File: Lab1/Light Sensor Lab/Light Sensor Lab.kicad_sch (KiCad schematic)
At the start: 9 parts, among them J1 Conn_01x03, U1 LMC6482

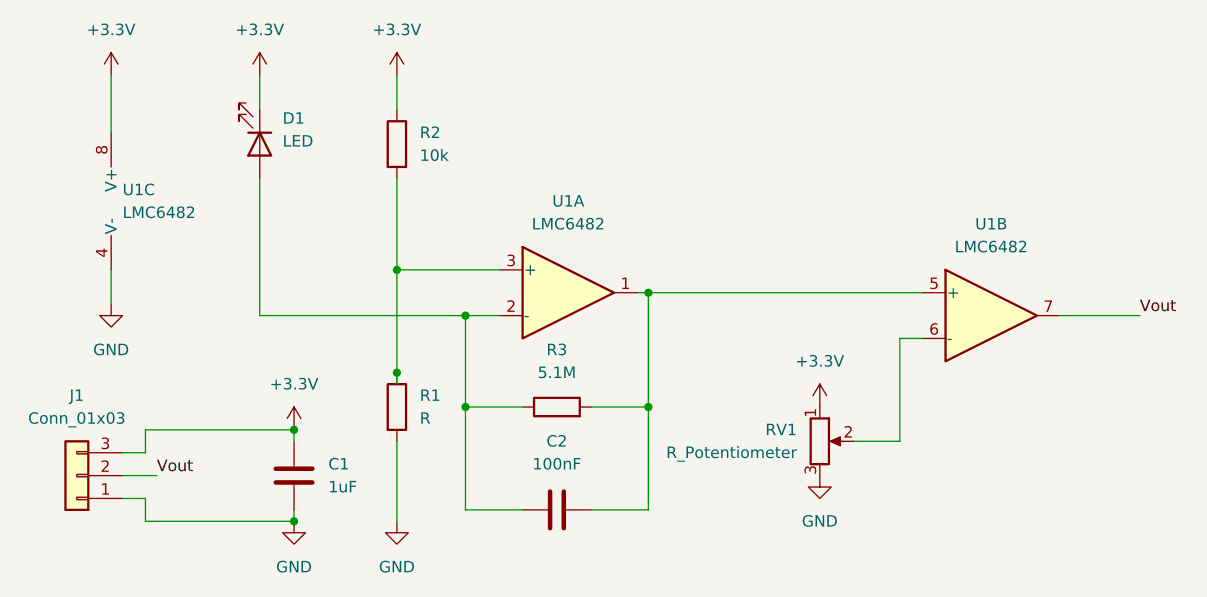
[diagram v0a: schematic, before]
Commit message: added PWR_FLAG for ERC
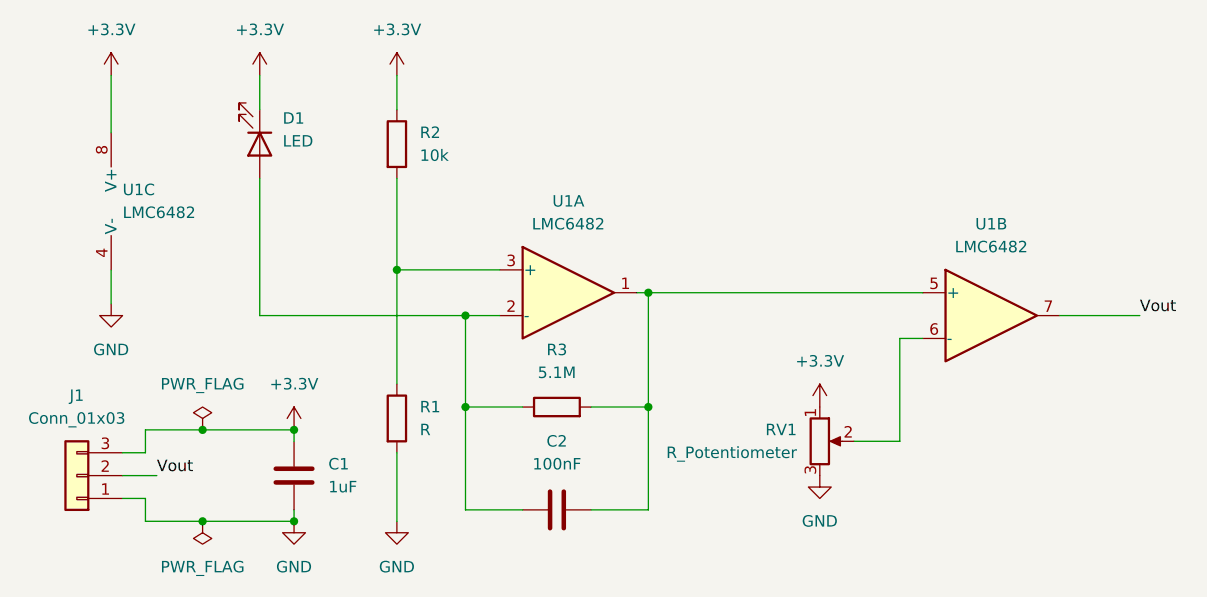
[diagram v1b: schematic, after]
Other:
- moved on the sheet: R1

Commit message: Finished Schematic And Checked Off
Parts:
- R1: value R -> 10k
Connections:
- net +3.3V: now also J1.1 (Pin_1), RV1.3; no longer J1.3 (Pin_3), RV1.1
- net GND: now also J1.3 (Pin_3), RV1.1; no longer J1.1 (Pin_1), RV1.3
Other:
- moved on the sheet: J1
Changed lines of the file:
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@@
+	(wire
+		(pts
+			(xy 153.67 101.6) (xy 153.67 104.14)
+		)
+		(stroke
+			(width 0)
+			(type default)
+		)
+	)
 	(wire
 		(pts
 			(xy 78.74 114.3) (xy 78.74 116.84)
+		)
+		(stroke
+			(width 0)
+			(type default)
+		)
+	)
+	(wire
+		(pts
+			(xy 153.67 114.3) (xy 153.67 111.76)
 		)
 		(stroke
@@
 		(lib_id "Device:R_Potentiometer")
 		(at 153.67 107.95 0)
-		(unit 1)
-		(exclude_from_sim no)
-		(in_bom yes)
-		(on_board yes)
-		(dnp no)
-		(fields_autoplaced yes)
+		(mirror x)
+		(unit 1)
+		(exclude_from_sim no)
+		(in_bom yes)
+		(on_board yes)
+		(dnp no)
 		(property "Reference" "RV1"
-			(at 151.13 106.6799 0)
+			(at 151.13 109.2201 0)
 			(effects
 				(font
@@
 		)
 		(property "Value" "R_Potentiometer"
-			(at 151.13 109.2199 0)
+			(at 151.13 106.6801 0)
 			(effects
 				(font
@@
 	(symbol
 		(lib_id "power:GND")
-		(at 153.67 111.76 0)
+		(at 153.67 114.3 0)
 		(unit 1)
 		(exclude_from_sim no)
@@
 		(fields_autoplaced yes)
 		(property "Reference" "#PWR05"
-			(at 153.67 118.11 0)
+			(at 153.67 120.65 0)
 			(effects
 				(font
@@
 		)
 		(property "Value" "GND"
-			(at 153.67 116.84 0)
-			(effects
-				(font
-					(size 1.27 1.27)
-				)
-			)
-		)
-		(property "Footprint" ""
-			(at 153.67 111.76 0)
+			(at 153.67 119.38 0)
+			(effects
+				(font
+					(size 1.27 1.27)
+				)
+			)
+		)
+		(property "Footprint" ""
+			(at 153.67 114.3 0)
 			(effects
 				(font
@@
 		)
 		(property "Datasheet" ""
-			(at 153.67 111.76 0)
+			(at 153.67 114.3 0)
 			(effects
 				(font
@@
 		)
 		(property "Description" "Power symbol creates a global label with name \"GND\" , ground"
-			(at 153.67 111.76 0)
+			(at 153.67 114.3 0)
 			(effects
 				(font
@@
 	(symbol
 		(lib_id "power:+3.3V")
-		(at 153.67 104.14 0)
+		(at 153.67 101.6 0)
 		(unit 1)
 		(exclude_from_sim no)
@@
 		(fields_autoplaced yes)
 		(property "Reference" "#PWR09"
-			(at 153.67 107.95 0)
+			(at 153.67 105.41 0)
 			(effects
 				(font
@@
 		)
 		(property "Value" "+3.3V"
-			(at 153.67 99.06 0)
-			(effects
-				(font
-					(size 1.27 1.27)
-				)
-			)
-		)
-		(property "Footprint" ""
-			(at 153.67 104.14 0)
+			(at 153.67 96.52 0)
+			(effects
+				(font
+					(size 1.27 1.27)
+				)
+			)
+		)
+		(property "Footprint" ""
+			(at 153.67 101.6 0)
 			(effects
 				(font
@@
 		)
 		(property "Datasheet" ""
-			(at 153.67 104.14 0)
+			(at 153.67 101.6 0)
 			(effects
 				(font
@@
 		)
 		(property "Description" "Power symbol creates a global label with name \"+3.3V\""
-			(at 153.67 104.14 0)
+			(at 153.67 101.6 0)
 			(effects
 				(font
@@
 			)
 		)
-		(property "Value" "R"
+		(property "Value" "10k"
 			(at 109.22 106.6799 0)
 			(effects
@@
 	(symbol
 		(lib_id "Connector_Generic:Conn_01x03")
-		(at 71.12 111.76 180)
-		(unit 1)
-		(exclude_from_sim no)
-		(in_bom yes)
-		(on_board yes)
-		(dnp no)
-		(fields_autoplaced yes)
+		(at 71.12 111.76 0)
+		(mirror y)
+		(unit 1)
+		(exclude_from_sim no)
+		(in_bom yes)
+		(on_board yes)
+		(dnp no)
 		(property "Reference" "J1"
+			(at 71.12 105.41 0)
+			(effects
+				(font
+					(size 1.27 1.27)
+				)
+			)
+		)
+		(property "Value" "Conn_01x03"
 			(at 71.12 102.87 0)
 			(effects
 				(font
-					(size 1.27 1.27)
-				)
-			)
-		)
-		(property "Value" "Conn_01x03"
-			(at 71.12 105.41 0)
-			(effects
-				(font

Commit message: PCB Layout done, DRC Approved, Awaiting Checkoff
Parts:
- C1, C2: footprint (none) -> Capacitor_SMD:C_0805_2012Metric
- D1: footprint (none) -> LED_THT:LED_D5.0mm
- J1: footprint (none) -> Connector_PinSocket_2.54mm:PinSocket_1x03_P2.54mm_Vertical
- R1, R2, R3: footprint (none) -> Resistor_THT:R_Axial_DIN0207_L6.3mm_D2.5mm_P7.62mm_Horizontal
- RV1: footprint (none) -> Potentiometer_THT:Potentiometer_Vishay_T7-YA_Single_Vertical
- U1: footprint (none) -> Package_SO:SOIC-8_3.9x4.9mm_P1.27mm
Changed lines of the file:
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@@
 			)
 		)
-		(property "Footprint" ""
+		(property "Footprint" "Capacitor_SMD:C_0805_2012Metric"
 			(at 96.2152 115.57 0)
 			(effects
@@
 			)
 		)
-		(property "Footprint" ""
+		(property "Footprint" "Potentiometer_THT:Potentiometer_Vishay_T7-YA_Single_Vertical"
 			(at 153.67 107.95 0)
 			(effects
@@
 			)
 		)
-		(property "Footprint" ""
+		(property "Footprint" "Package_SO:SOIC-8_3.9x4.9mm_P1.27mm"
 			(at 77.47 81.28 0)
 			(effects
@@
 			)
 		)
-		(property "Footprint" ""
+		(property "Footprint" "Resistor_THT:R_Axial_DIN0207_L6.3mm_D2.5mm_P7.62mm_Horizontal"
 			(at 104.902 74.93 90)
 			(effects
@@
 			)
 		)
-		(property "Footprint" ""
+		(property "Footprint" "Capacitor_SMD:C_0805_2012Metric"
 			(at 128.27 114.6048 0)
 			(effects
@@
 			)
 		)
-		(property "Footprint" ""
+		(property "Footprint" "Resistor_THT:R_Axial_DIN0207_L6.3mm_D2.5mm_P7.62mm_Horizontal"
 			(at 104.902 105.41 90)
 			(effects
@@
 			)
 		)
-		(property "Footprint" ""
+		(property "Footprint" "Package_SO:SOIC-8_3.9x4.9mm_P1.27mm"
 			(at 125.73 91.44 0)
 			(effects
@@
 			)
 		)
-		(property "Footprint" ""
+		(property "Footprint" "Connector_PinSocket_2.54mm:PinSocket_1x03_P2.54mm_Vertical"
 			(at 71.12 111.76 0)
 			(effects
@@
 			)
 		)
-		(property "Footprint" ""
+		(property "Footprint" "LED_THT:LED_D5.0mm"
 			(at 91.44 74.93 0)
 			(effects
@@
 			)
 		)
-		(property "Footprint" ""
+		(property "Footprint" "Package_SO:SOIC-8_3.9x4.9mm_P1.27mm"
 			(at 172.72 93.98 0)
 			(effects
@@
 			)
 		)
-		(property "Footprint" ""
+		(property "Footprint" "Resistor_THT:R_Axial_DIN0207_L6.3mm_D2.5mm_P7.62mm_Horizontal"
 			(at 124.46 105.918 90)
 			(effects
